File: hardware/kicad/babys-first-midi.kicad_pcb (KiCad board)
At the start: 2 copper layers, 120 x 80 mm, 26 parts, among them J1 BFM:RJ45_Generic_THT, J2 Connector_Audio:TRS_3.5mm_Hor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, Q1 Package_TO_SOT_THT:TO-220-3_V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, Q2 Package_TO_SOT_THT:TO-220-3_V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, Q3 Package_TO_SOT_THT:TO-220-3_V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, Q4 Package_TO_SOT_THT:TO-220-3_V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, Q5 Package_TO_SOT_THT:TO-220-3_V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, U1 BFM:Pimoroni_Tiny2350_2x8_Hea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

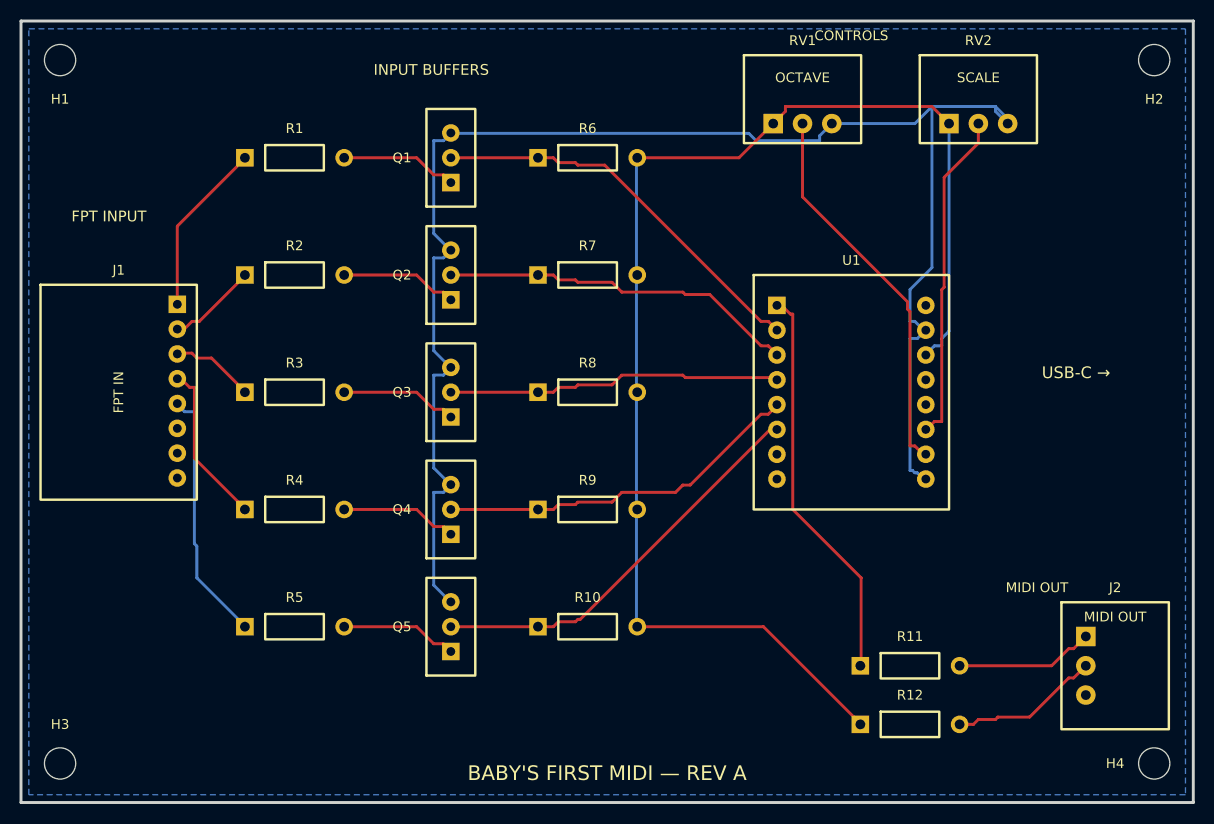
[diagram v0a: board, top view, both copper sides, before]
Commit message: Fit WH148 pots and correct Tiny 2350 pin banks with drawing-based models
Replace 3 mm pot pads with 5 mm pitch and 1.3 mm holes for direct horizontal mounting. Correct the Tiny module banks, orient USB toward the right edge, and attach detailed drawing-based models. Reroute and refill while preserving all 26 components and numbered pad net assignments.

KiCad 10.0.6: zero DRC violations and zero unconnected items. Document sources, assumed assembly heights, and remaining connector model limitations.
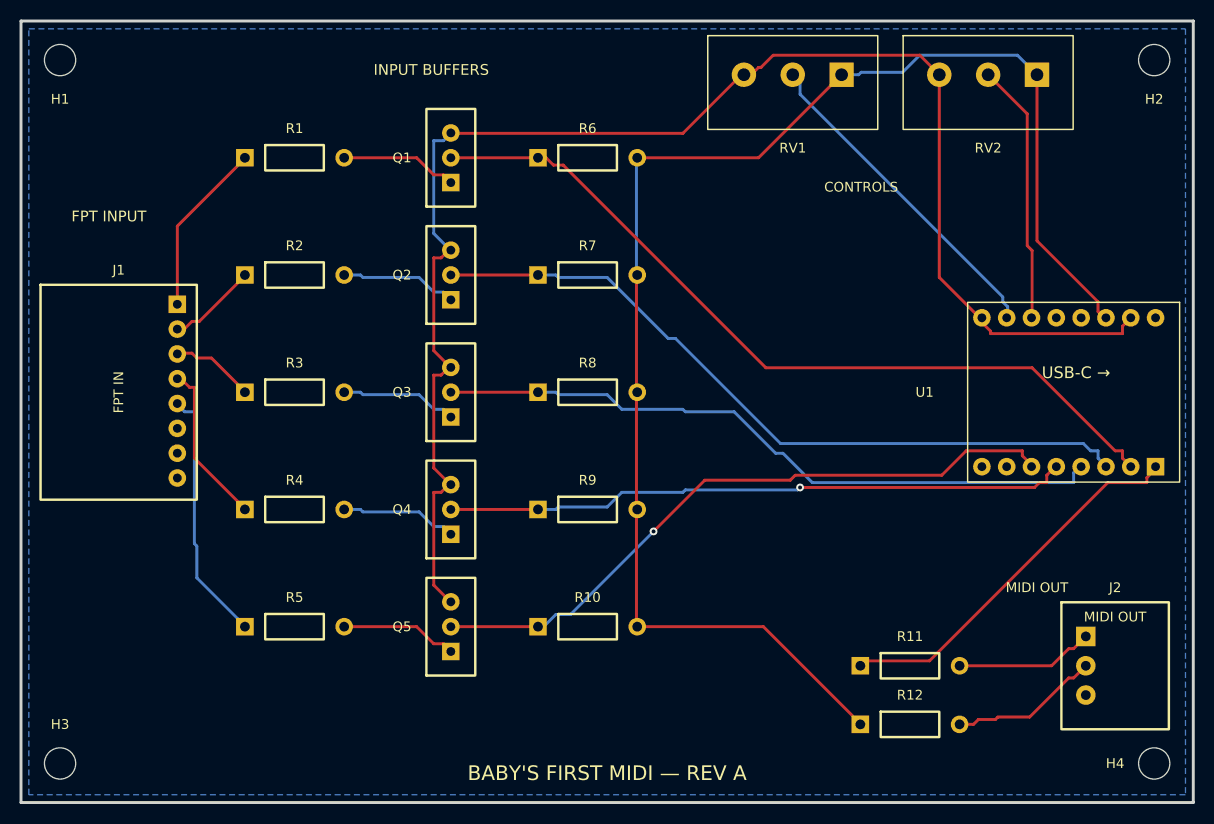
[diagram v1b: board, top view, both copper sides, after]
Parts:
- RV1, RV2: value Potentiometer_THT:RK09K_Horizontal -> 10k; footprint BFM:RK09K_Horizontal -> BFM:WH148_Horizontal_P5.00mm
- moved U1 22.2 mm to (127.2, 58.0), turned to -90 degrees
- moved RV1 2.69 mm to (99.0, 25.5)
- moved RV2 2.69 mm to (119.0, 25.5)
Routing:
- net KEY_C: track 41.2 -> 83.3 mm
- net KEY_D: track 37.2 -> 75.8 mm
- net KEY_E: track 34.7 -> 69.9 mm
- net KEY_F: track 38.2 -> 64.6 mm, vias 0 -> 1
- net KEY_G: track 42.2 -> 68.2 mm, vias 0 -> 1
- net 3V3: track 136.6 -> 150.2 mm
- net GND: track 167.9 -> 155.1 mm
- net ADC_SCALE: track 34.2 -> 27.0 mm
- net ADC_OCTAVE: track 39.5 -> 34.3 mm
- net MIDI_TX: track 41.1 -> 39.4 mm

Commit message: Replace MIDI jack with PJ-320A footprint and STEP model
Apply the supplied uxcell pinout: pin 4 MIDI_TIP, pin 3 MIDI_RING, pin 2 unused and pin 1 sleeve unconnected as in the prior design. Adapt Keebio's footprint silkscreen, preserve its MIT attribution, and place the jack opening at the right board edge.

Reroute and refill copper. KiCad 10.0.6 reports zero violations and zero unconnected items; all connections outside J2 and all 26 components are preserved. Document the community model's mechanical verification limits.
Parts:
- J2: value Connector_Audio:TRS_3.5mm_Horizontal -> PJ-320A; footprint BFM:TRS_3.5mm_Horizontal -> BFM:PJ320A_Uxcell_Horizontal
- moved J2 6.00 mm to (138.0, 86.0), turned to -90 degrees
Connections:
- J2 pad 1: MIDI_TIP -> (no net)
- J2 pad 2: MIDI_RING -> (no net)
- J2 pad 3: (no net) -> MIDI_RING
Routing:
- net MIDI_TIP: track 14.3 -> 21.6 mm
- net MIDI_RING: track 15.6 -> 17.5 mm

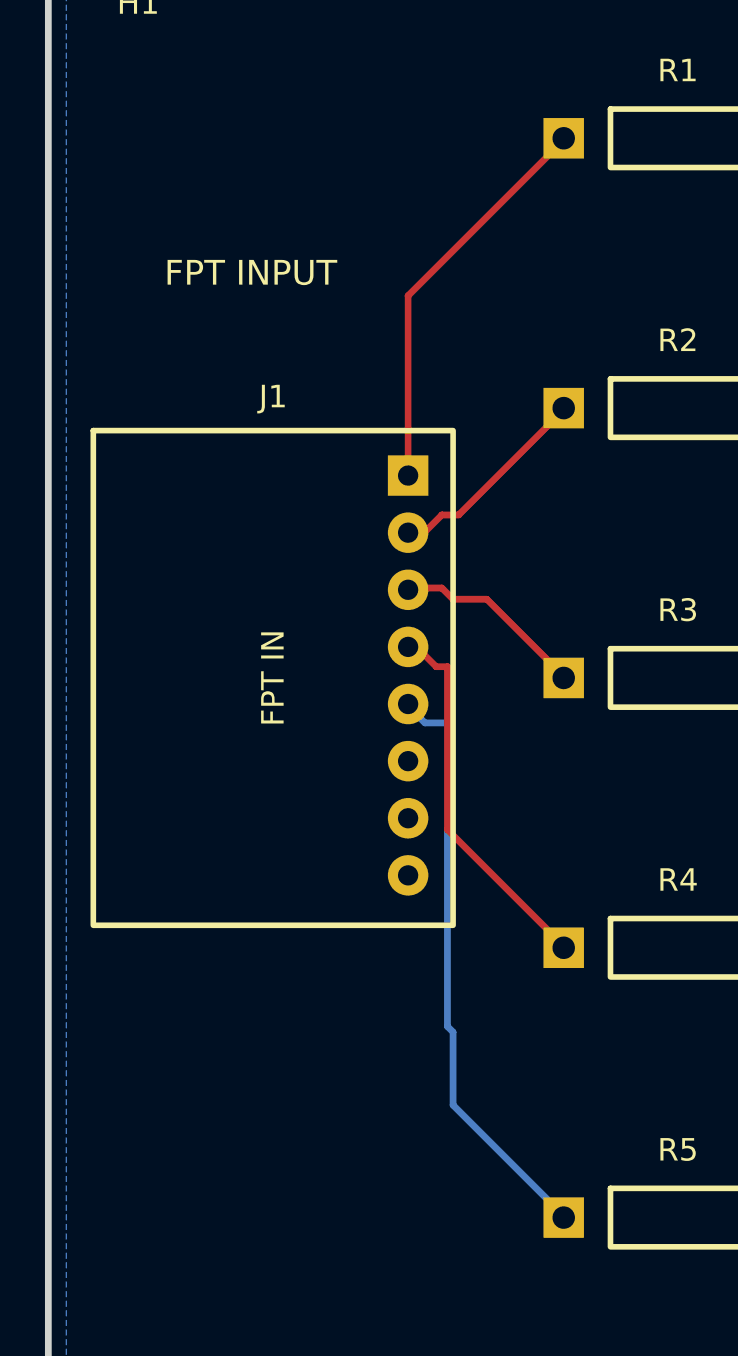
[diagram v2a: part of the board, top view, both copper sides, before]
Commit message: Fit drawing-based RJ45 connector with documented prototype pinout
Replace J1's placeholder with the FMHXG mechanical footprint and custom 3D model, facing the left board edge. Use the user-approved provisional sequential contact numbering and preserve existing numbered signal nets. Leave shield pads unconnected and include an exact continuity-check guide for verification when the physical parts arrive.

Reroute and refill. KiCad 10.0.6 reports zero violations and zero unconnected items; all 26 components and existing numbered pad net assignments are preserved. Physical contact numbering remains an assumption, not a verified manufacturer pinout.
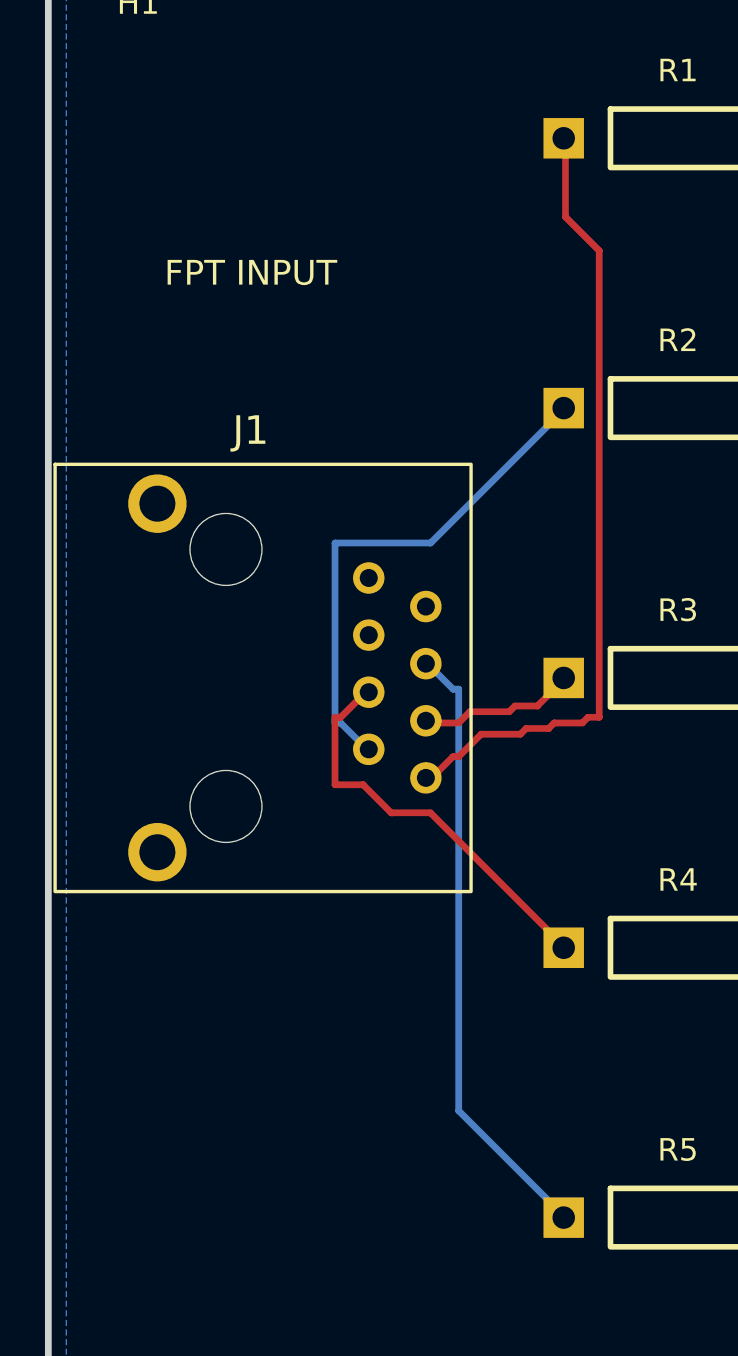
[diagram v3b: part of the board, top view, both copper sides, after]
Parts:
- J1: value BFM:RJ45_Generic_THT -> RJ45NMCCFC-90D-10; footprint BFM:RJ45_Generic_THT -> BFM:RJ45_FMHXG_AssumedPinout
- moved J1 10.0 mm to (20.0, 58.0), turned to 90 degrees
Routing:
- net FPT_C: track 18.0 -> 35.4 mm
- net FPT_D: track 9.40 -> 22.9 mm
- net FPT_E: track 8.82 -> 7.26 mm
- net FPT_F: track 17.0 -> 18.4 mm
- net FPT_G: track 26.4 -> 27.7 mm

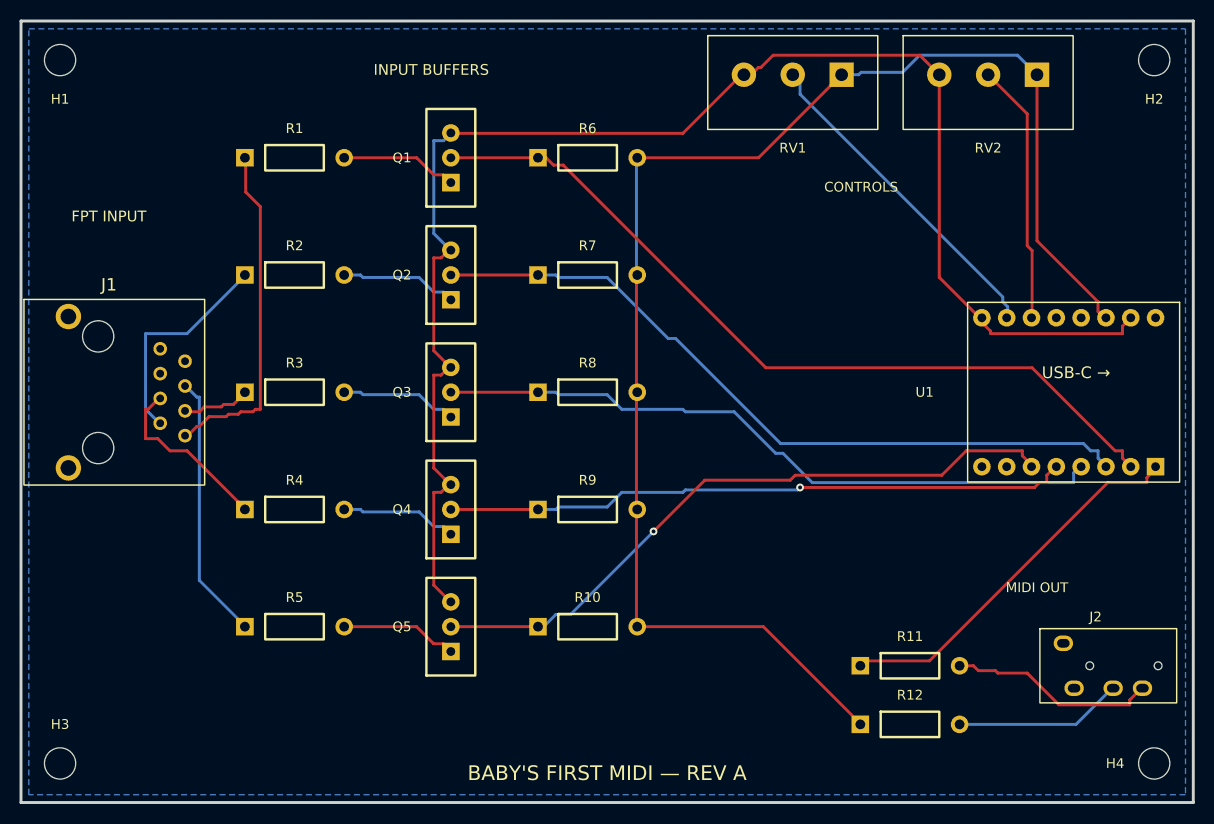
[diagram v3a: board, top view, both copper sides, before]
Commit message: Replace input MOSFETs with through-hole 2N7000 TO-92 parts
Replace Q1-Q5 IRLZ44N packages with local TO-92 footprints at 2.54 mm lead spacing and standard KiCad 3D models. Remap source/gate/drain to pins 1/2/3 in PCB and embedded schematic symbol while preserving connections by function. Reroute and refill the PCB.

Verified all component PCB net assignments and before/after schematic netlists with the functional pin remap. KiCad 10.0.6 DRC: zero violations, zero unconnected items.
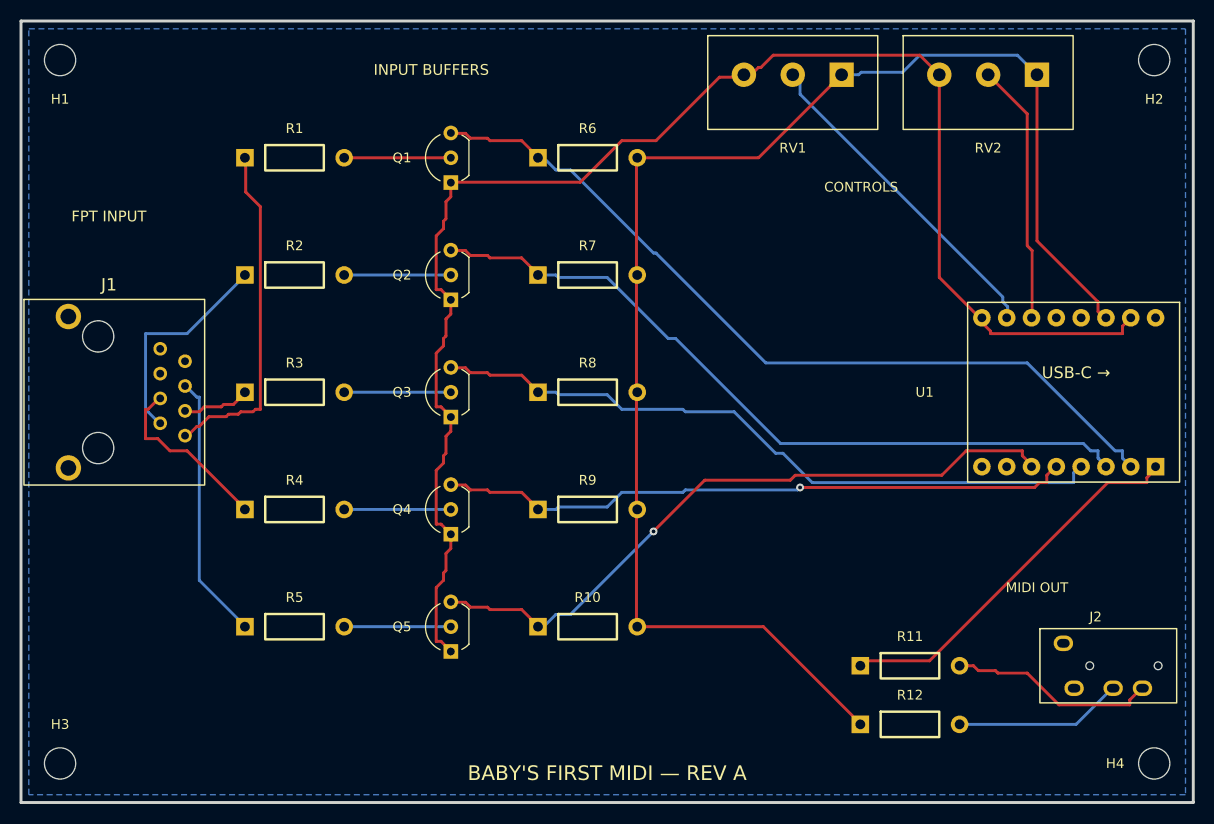
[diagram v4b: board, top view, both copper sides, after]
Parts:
- Q1, Q2, Q3, Q4, Q5: value Package_TO_SOT_THT:TO-220-3_Vertical -> 2N7000; footprint BFM:TO-220-3_Vertical -> BFM:TO-92_2N7000_SGD
- moved Q4 2.54 mm to (64.0, 72.5)
- moved Q5 2.54 mm to (64.0, 84.5)
- moved Q1 2.54 mm to (64.0, 36.5)
- moved Q2 2.54 mm to (64.0, 48.5)
- moved Q3 2.54 mm to (64.0, 60.5)
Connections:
- Q1 pad 1: GATE_C -> GND
- Q1 pad 2: KEY_C -> GATE_C
- Q1 pad 3: GND -> KEY_C
- Q2 pad 1: GATE_D -> GND
- Q2 pad 2: KEY_D -> GATE_D
- Q2 pad 3: GND -> KEY_D
- Q3 pad 1: GATE_E -> GND
- Q3 pad 2: KEY_E -> GATE_E
- Q3 pad 3: GND -> KEY_E
- Q4 pad 1: GATE_F -> GND
- Q4 pad 2: KEY_F -> GATE_F
- Q4 pad 3: GND -> KEY_F
- Q5 pad 1: GATE_G -> GND
- Q5 pad 2: KEY_G -> GATE_G
- Q5 pad 3: GND -> KEY_G
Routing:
- net KEY_G: track 68.2 -> 69.2 mm
- net KEY_F: track 64.6 -> 65.7 mm
- net KEY_C: track 83.3 -> 84.4 mm
- net GATE_G: track 12.2 -> 11.1 mm
- net GATE_F: track 12.2 -> 11.1 mm
- net GATE_E: track 12.2 -> 11.1 mm
- net GATE_D: track 12.2 -> 11.1 mm
- net GATE_C: track 12.2 -> 11.1 mm
- net KEY_D: track 75.8 -> 76.9 mm
- net KEY_E: track 69.9 -> 71.0 mm
